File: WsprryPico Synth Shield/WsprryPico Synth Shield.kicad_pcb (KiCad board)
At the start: 2 copper layers, 53.3 x 22.9 mm, 1 part

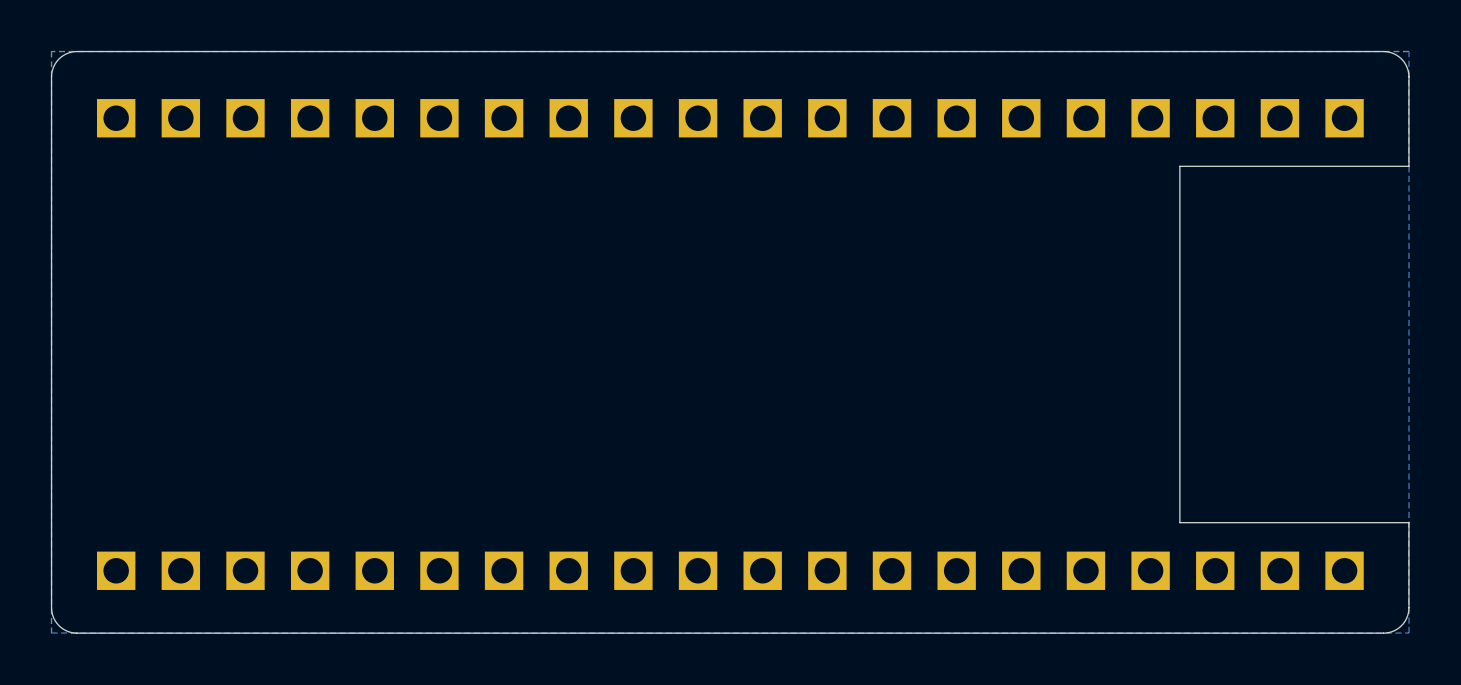
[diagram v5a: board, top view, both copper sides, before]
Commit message: Checked through the JLCPCB upload
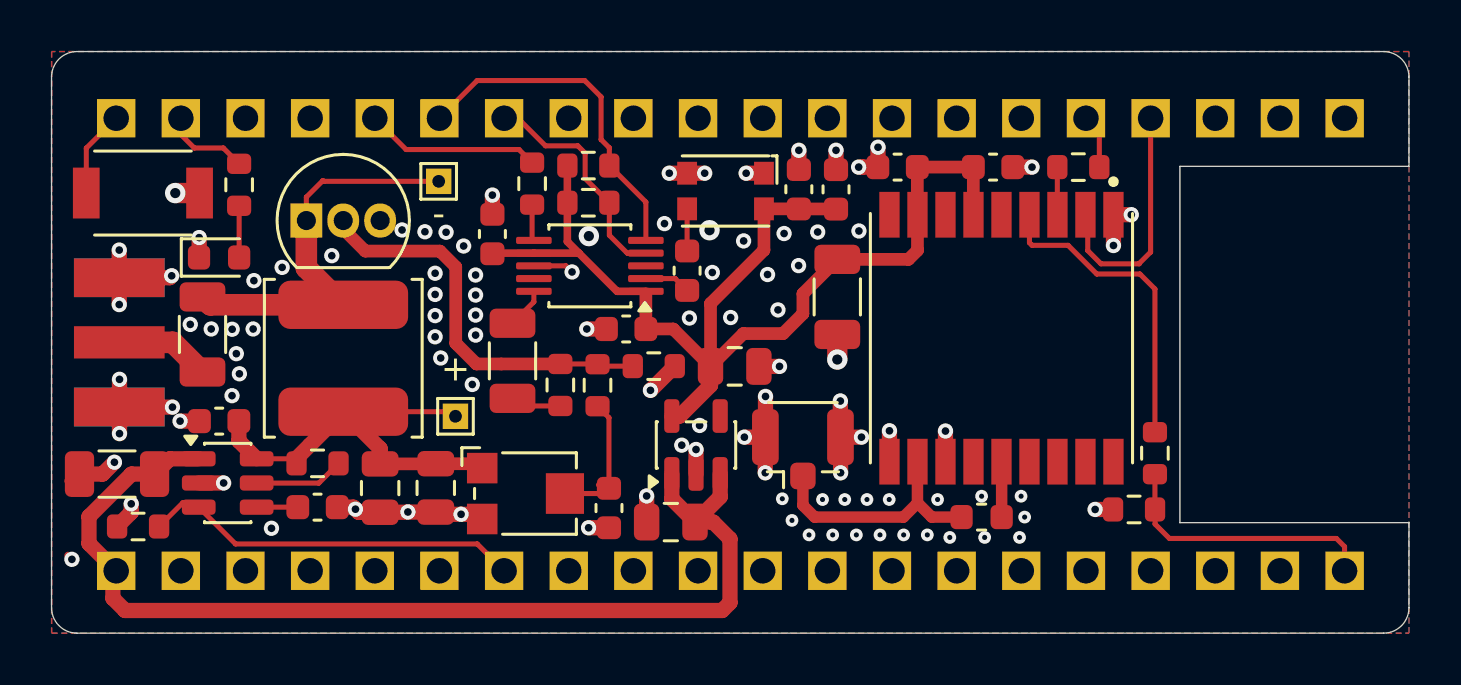
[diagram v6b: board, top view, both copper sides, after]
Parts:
- added C21: 2.2μF, wsprrypico-synth-shield:C_0805_2012Metric, F.Cu at (144.5, 96.8)
- added C22: 2.2μF, wsprrypico-synth-shield:C_0805_2012Metric, F.Cu at (147.0, 90.7)
- added C31: 10μF, wsprrypico-synth-shield:C_1206_3216Metric, F.Cu at (122.7, 95.0)
- added C32: 1nF, wsprrypico-synth-shield:C_0603_1608Metric, F.Cu at (130.6, 96.2)
- added C33: 1μF, wsprrypico-synth-shield:C_0805_2012Metric, F.Cu at (133.0, 95.5)
- added C41: 10nF, wsprrypico-synth-shield:C_0603_1608Metric, F.Cu at (149.5, 83.8)
- added C42: 1nF, wsprrypico-synth-shield:C_0603_1608Metric, F.Cu at (145.1, 87.0)
- added C43: 100nF, wsprrypico-synth-shield:C_0603_1608Metric, F.Cu at (150.9, 83.8)
- added C51: 100nF, wsprrypico-synth-shield:C_0603_1608Metric, F.Cu at (137.4, 85.5)
- added C52: 100nF, wsprrypico-synth-shield:C_0603_1608Metric, F.Cu at (142.7, 89.2)
- added C61: 100nF, wsprrypico-synth-shield:C_1206_3216Metric, F.Cu at (138.2, 90.5)
- added C62: 100nF, wsprrypico-synth-shield:C_0603_1608Metric, F.Cu at (126.7, 92.9)
- added C63: 1μF, wsprrypico-synth-shield:C_0805_2012Metric, F.Cu at (135.2, 95.5)
- added C64: 100nF, wsprrypico-synth-shield:C_1206_3216Metric, F.Cu at (126.1, 89.5)
- added C65: 100nF, wsprrypico-synth-shield:C_0603_1608Metric, F.Cu at (142.0, 96.3)
- added C71: 10μF, wsprrypico-synth-shield:C_1206_3216Metric, F.Cu at (151.0, 88.0)
- added C72: 100nF, wsprrypico-synth-shield:C_0603_1608Metric, F.Cu at (153.4, 82.9)
- added C73: 100nF, wsprrypico-synth-shield:C_0603_1608Metric, F.Cu at (157.1, 82.9)
- added D11: Red, wsprrypico-synth-shield:LED_0603_1608Metric, F.Cu at (126.7, 86.4)
- added J61: SMA 50ohm, wsprrypico-synth-shield:SMA_Adafruit_1865_EdgeMount, F.Cu at (120.5, 89.8)
- added J71: U.FL 50ohm, wsprrypico-synth-shield:U.FL_Hirose_U.FL-R-SMT-1_Vertical, F.Cu at (149.7, 93.5)
- added L61: 330uH, wsprrypico-synth-shield:L_TDK_VLS6045EX_VLS6045AF, F.Cu at (131.6, 90.4)
- added L71: 47nH, wsprrypico-synth-shield:L_0603_1608Metric, F.Cu at (156.7, 96.6)
- added Q61: BS170, wsprrypico-synth-shield:TO-92_Inline, F.Cu at (130.3, 85.0)
- added R11: 1kΩ, wsprrypico-synth-shield:R_0603_1608Metric, F.Cu at (127.5, 83.6)
- added R31: 100kΩ, wsprrypico-synth-shield:R_0603_1608Metric, F.Cu at (123.5, 97.0)
- added R32: 1kΩ, wsprrypico-synth-shield:R_0603_1608Metric, F.Cu at (130.6, 94.5)
- added R51: 4.7kΩ, wsprrypico-synth-shield:R_0603_1608Metric, F.Cu at (141.2, 82.8)
- added R52: 4.7kΩ, wsprrypico-synth-shield:R_0603_1608Metric, F.Cu at (141.2, 84.3)
- added R53: 33Ω, wsprrypico-synth-shield:R_0603_1608Metric, F.Cu at (139.0, 83.5)
- added R61: 22Ω, wsprrypico-synth-shield:R_0603_1608Metric, F.Cu at (140.1, 91.5)
- added R62: 4.7kΩ, wsprrypico-synth-shield:R_0603_1608Metric, F.Cu at (141.6, 91.5)
- added R63: 100kΩ, wsprrypico-synth-shield:R_0603_1608Metric, F.Cu at (143.8, 90.7)
- added R71: 1kΩ, wsprrypico-synth-shield:R_0603_1608Metric, F.Cu at (160.5, 82.9)
- added R72: 100kΩ, wsprrypico-synth-shield:R_0603_1608Metric, F.Cu at (162.7, 96.3)
- added R73: 1kΩ, wsprrypico-synth-shield:R_0603_1608Metric, F.Cu at (163.5, 94.1)
- added RV61: 5kΩ, wsprrypico-synth-shield:Potentiometer_Bourns_TC33X_Vertical, F.Cu at (138.8, 95.7)
- added SW11: Push, wsprrypico-synth-shield:SW_SPST_XUNPU_TS1088R_4x3mm, F.Cu at (123.7, 83.9)
- added TP61: +, wsprrypico-synth-shield:TestPoint_THTPad_1.0x1.0mm_Drill0.5mm, F.Cu at (136.0, 92.7)
- added TP62: -, wsprrypico-synth-shield:TestPoint_THTPad_1.0x1.0mm_Drill0.5mm, F.Cu at (135.3, 83.5)
- added U21: TPS7A2033, wsprrypico-synth-shield:SOT-23-5, F.Cu at (145.4, 93.8)
- added U31: TPS22918, wsprrypico-synth-shield:SOT-23-6, F.Cu at (127.1, 95.3)
- added U51: Si5351A-B-GTR, wsprrypico-synth-shield:MSOP-10_Si5351A_3x3mm_P0.5mm, F.Cu at (141.3, 86.8)
- added U71: ATGM336H-5N31, wsprrypico-synth-shield:Zhongke_ATGM336H-5N31_9.7x10.1mm_P1.1mm, F.Cu at (157.4, 89.6)
- added Y41: 25MHz TCXO, wsprrypico-synth-shield:KDS_DSB321SDN_3.2x2.5mm, F.Cu at (146.6, 83.8)
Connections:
- U11 pad 1: /GPS_RX -> /BUTTON
- U11 pad 14: /COUNTER_SCK -> unconnected-(U11-GP10-Pad14)
- U11 pad 15: /COUNTER_MOSI -> unconnected-(U11-GP11-Pad15)
- U11 pad 16: /COUNTER_MISO -> /GPS_RX
- U11 pad 17: /COUNTER_CS_N -> /GPS_TX
- U11 pad 19: /BUTTON_N -> unconnected-(U11-GP14-Pad19)
- U11 pad 2: /GPS_TX -> /LED_DRIVE
- U11 pad 20: /LED_DRIVE -> unconnected-(U11-GP15-Pad20)
- U11 pad 22: /COUNTER_IRQ_N -> unconnected-(U11-GP17-Pad22)
- U11 pad 34: unconnected-(U11-GP28/ADC2-Pad34) -> /AMP_EN
- U11 pad 36: /PICO_3V3 -> unconnected-(U11-3V3_OUT-Pad36)
- U11 pad 39: /VSYS -> unconnected-(U11-VSYS-Pad39)
- U11 pad 5: unconnected-(U11-GP3-Pad5) -> /SYNTH_CLK2_FB
- U11 pad 9: /AMP_EN -> unconnected-(U11-GP6-Pad9)
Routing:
- net GND: track 0.00 -> 48.8 mm, vias 0 -> 103
- net /SYNTH_3V3: track 0.00 -> 45.3 mm
- net /VBUS: track 0.00 -> 42.3 mm
- net /AMP_5V_SW: track 0.00 -> 17.7 mm
- net /AMP_DRAIN: track 0.00 -> 16.0 mm
- net /AMP_GATE: track 0.00 -> 15.7 mm
- net /AMP_EN: track 0.00 -> 15.0 mm
- net /SYNTH_SDA: track 0.00 -> 13.6 mm
- net /GPS_PPS_RAW: track 0.00 -> 12.4 mm
- net /GPS_PPS: track 0.00 -> 10.7 mm
- net /GPS_ANT: track 0.00 -> 9.66 mm
- net /GPS_TX: track 0.00 -> 9.55 mm
- net /SYNTH_SCL: track 0.00 -> 9.10 mm
- net /SYNTH_CLK2_FB: track 0.00 -> 6.90 mm
- net /AMP_BIAS: track 0.00 -> 5.71 mm
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- added copper zone on F.Cu, net GND
